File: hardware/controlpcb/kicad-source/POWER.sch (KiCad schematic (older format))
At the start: 37 parts, among them P1 WR-TBL_691313710002, Q1 IPD90P03P4L- 04, U5 OPA2374AIDCN, U6 IFX91041EFJ, U7 LM317

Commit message: added kicad source
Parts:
- removed D2, D3: Led_Small, LEDs:LED_0603, symbol devices:Led_Small
- removed R10: 10k, resistors:R_0603, symbol devices:R_0603
- removed R11, R12: 220, resistors:R_0603, symbol devices:R_0603
- removed R7: 100k, resistors:R_0603, symbol devices:R_0603
- removed U5: OPA2374AIDCN, SOIC:SOIC-8_3.9x4.9mm_Pitch1.27mm, symbol opamps:OPA2374AIDCN
- C10: value 100n -> 100nF
- F1: footprint fuse_holders_and_fuses:BladeFuse-CarType -> fuse_holders_and_fuses:Fuseholder_ATO_Blade_littlefuse_8_Pin
- R8: value 20k -> 150k
- R9: value 100k -> 20k
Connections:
- net +BATT: now also R8.1; no longer R9.1
- net GND: now also R9.2; no longer R8.2
- new net VBAT_SENSE: R8.2, R9.1
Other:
- moved on the sheet: C15, C16, R66, R67, U7

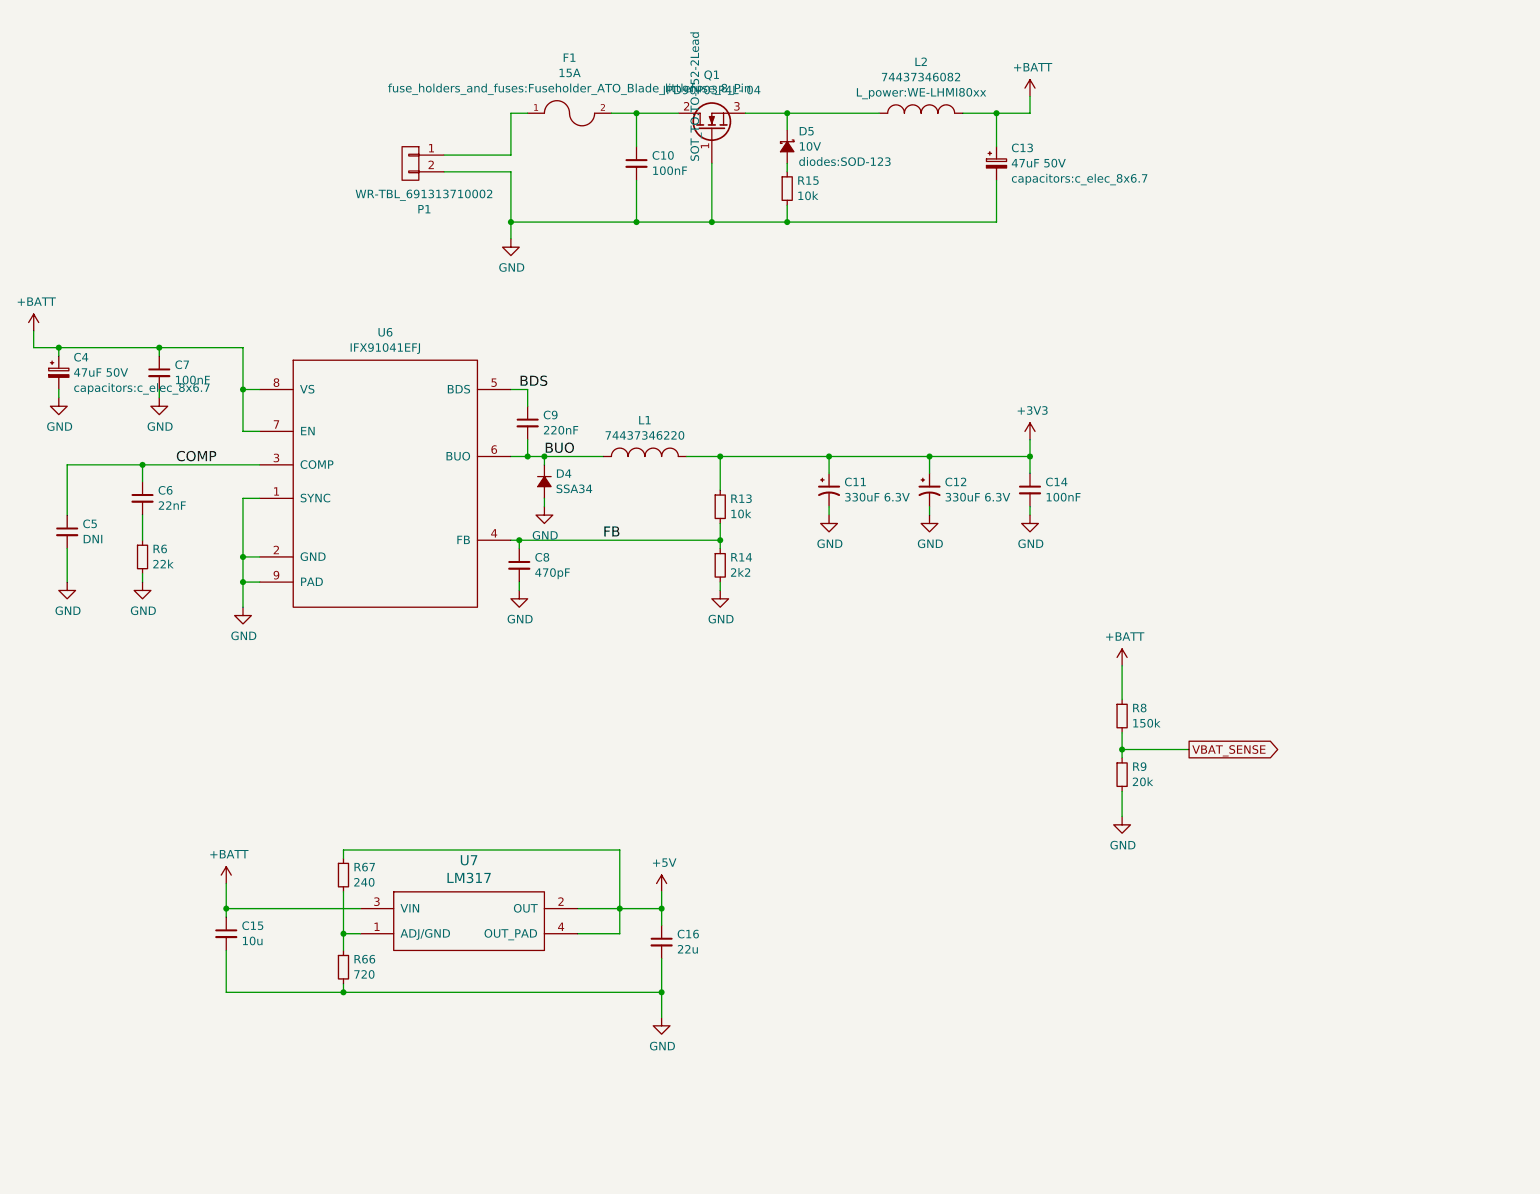
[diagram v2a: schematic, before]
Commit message: changed power supply
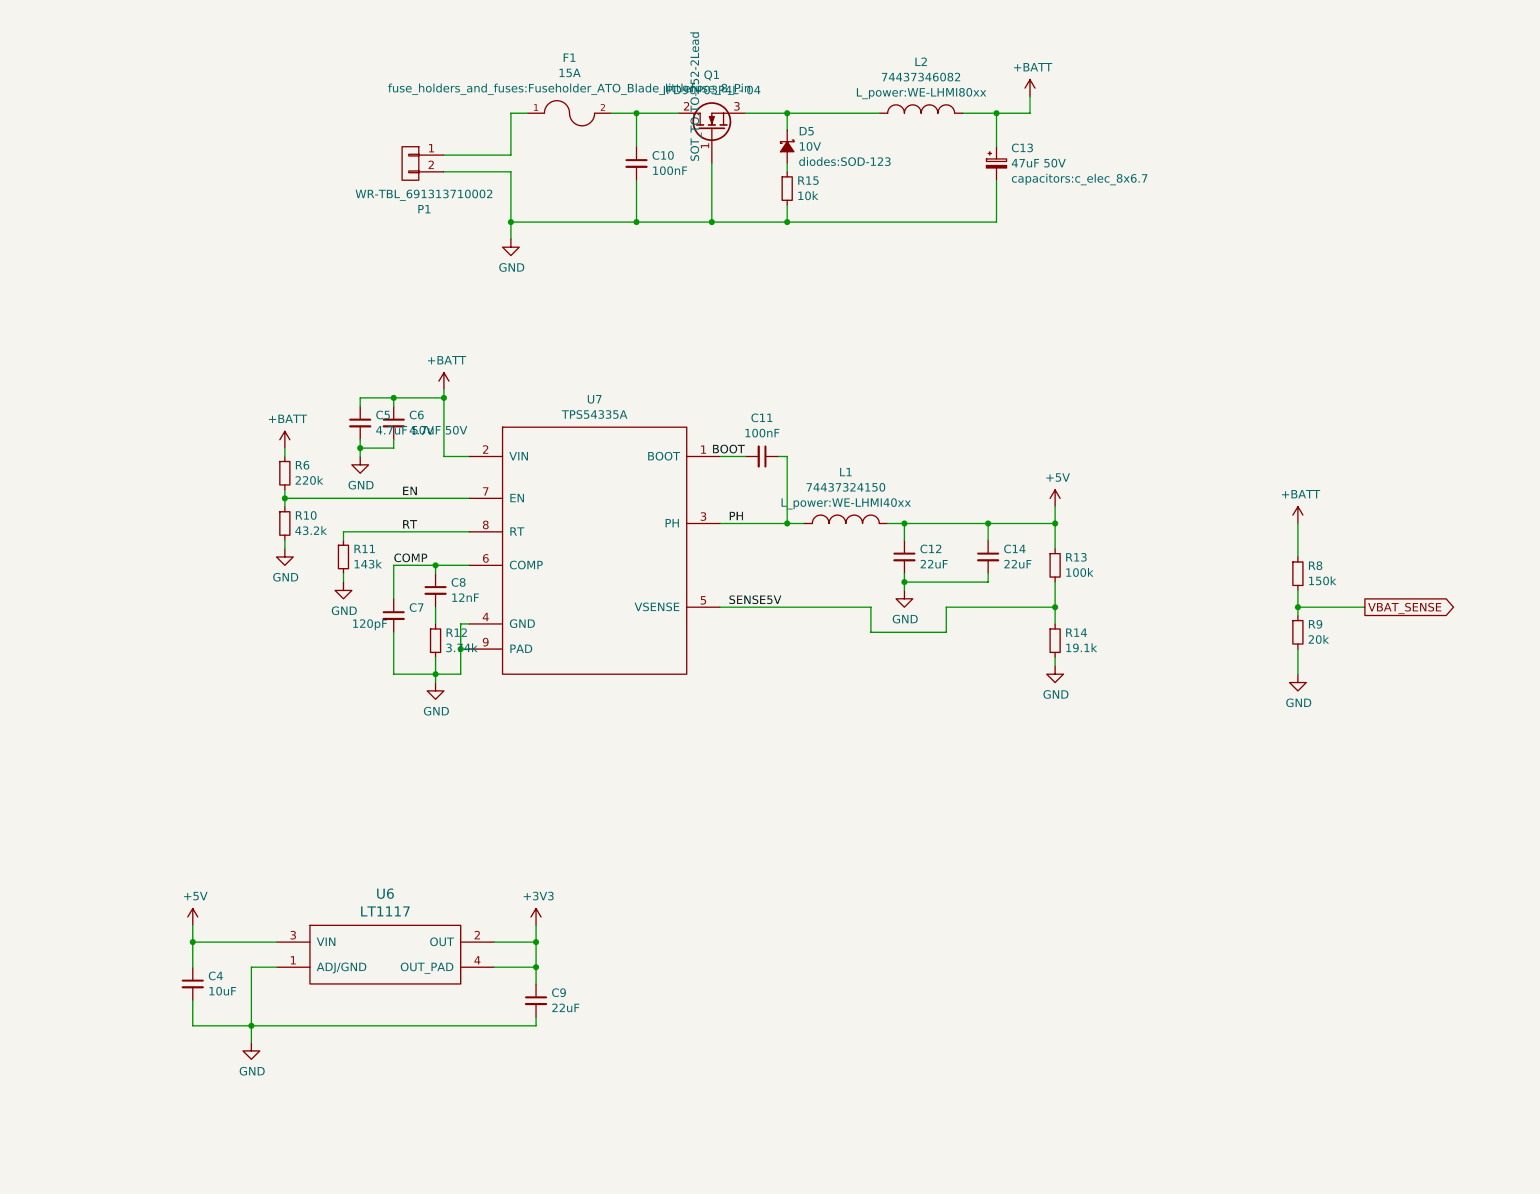
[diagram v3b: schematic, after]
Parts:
- removed C11, C12: 330uF 6.3V, capacitors:TantalC_SizeD_EIA-7343_Wave, symbol devices:CP1_Small
- removed C14: 100nF, capacitors:C_0603, symbol devices:C_0603
- removed C15: 10u, capacitors:C_0603, symbol devices:C_0603
- removed C16: 22u, capacitors:C_0603, symbol devices:C_0603
- removed C4: 47uF 50V, capacitors:c_elec_8x6.7, symbol devices:CP_Small
- removed C5: DNI, capacitors:C_0603, symbol devices:C_0603
- removed C6: 22nF, capacitors:C_0603, symbol devices:C_0603
- removed C9: 220nF, capacitors:C_0603, symbol devices:C_0603
- removed D4: SSA34, diodes:SMA_Standard, symbol devices:D_Small
- removed L1: 74437346220, L_power:WE-LHMI70xx, symbol L_power:74437346220
- removed R66: 720, resistors:R_0603, symbol devices:R_0603
- removed R67: 240, resistors:R_0603, symbol devices:R_0603
- removed U6: IFX91041EFJ, SOIC:SOIC-8-1EP_3.9x4.9mm_Pitch1.27mm, symbol voltage-regulators:IFX91041EFJ
- removed U7: LM317, SOT_TO:SOT-223, symbol voltage-regulators:LT1085
- added C11: 100nF, capacitors:C_0603, symbol devices:C_0603
- added C12, C14, C9: 22uF, capacitors:C_1206, symbol devices:C_1206
- added C4: 10uF, capacitors:C_1206, symbol devices:C_1206
- added C5, C6: 4.7uF 50V, capacitors:C_1206, symbol devices:C_1206
- added L1: 74437324150, L_power:WE-LHMI40xx, symbol L_power:74437346100
- added R10: 43.2k, resistors:R_0603, symbol devices:R_0603
- added R11: 143k, resistors:R_0603, symbol devices:R_0603
- added R12: 3.74k, resistors:R_0603, symbol devices:R_0603
- added U6: LT1117, SOT_TO:SOT-223, symbol voltage-regulators:LT1117
- added U7: TPS54335A, SOIC:SOIC-8-1EP_3.9x4.9mm_Pitch1.27mm, symbol voltage-regulators:TPS54335A
- C7: value 100nF -> 120pF
- C8: value 470pF -> 12nF
- R13: value 10k -> 100k
- R14: value 2k2 -> 19.1k
- R6: value 22k -> 220k
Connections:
- net +3V3: now also C9.1, U6.2 (OUT), U6.4 (OUT_PAD); no longer R13.1
- net +5V: now also R13.1, C12.1, C14.1, C4.1, L1.2, U6.3 (VIN)
- net +BATT: now also R6.1, C5.1, C6.1, U7.2 (VIN); no longer C7.1
- net COMP: now also C7.1, C8.1, U7.6 (COMP)
- net GND: now also C12.2, C14.2, C4.2, C5.2, C6.2, C9.2, R10.2, R11.2, R12.2, U6.1 (ADJ/GND), U7.4 (GND), U7.9 (PAD); no longer C8.2, R6.2
- net FB renamed SENSE5V
- net SENSE5V: now also U7.5 (VSENSE); no longer C8.1
- new net: C11.2, U7.1 (BOOT)
- new net: C8.2, R12.1
- new net EN: R10.1, R6.2, U7.7 (EN)
- new net PH: C11.1, L1.1, U7.3 (PH)
- new net RT: R11.1, U7.8 (RT)
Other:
- moved on the sheet: R8, R9
